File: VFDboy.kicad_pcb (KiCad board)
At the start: 2 copper layers, 141.2 x 60 mm, 161 parts, among them J1 AVR-ISP-6, J2 USB_C_Receptacle_USB2.0, J3 Micro_SD_Card_Det, J4 TagConnect_TC2030_SWD, Q1 FS8205A, Q2 S9015, Q3 AO3401A, Q4 AO3401A, Q5 S9015, Q6 2N7002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

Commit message: Add option for elevated D-Pad
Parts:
- added SW7: D-Pad, button-daughterboard:Daughterboard_D-Pad, F.Cu at (115.0, 129.9)
- moved D3 6.86 mm to (170.2, 104.1), turned to 180 degrees
- moved R2 3.01 mm to (168.0, 103.5), turned to 180 degrees
- moved R3 2.46 mm to (168.0, 104.6), turned to 180 degrees
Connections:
- U8 pad 42: /LEFT -> /DOWN
- U8 pad 43: /DOWN -> /LEFT
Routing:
- net Net-(D3-Pad2): track 12.4 -> 22.3 mm
- net +5V: track 508.2 -> 501.4 mm
- net /RIGHT: track 119.3 -> 121.7 mm
- net /DOWN: track 127.6 -> 125.4 mm
- net Net-(R2-Pad2): track 27.5 -> 29.4 mm
- net /LEFT: track 133.1 -> 134.4 mm
- net /UP: track 127.0 -> 126.3 mm
- net /Leds/Led 9/DIN: track 72.6 -> 72.0 mm
- net GND: vias 219 -> 272

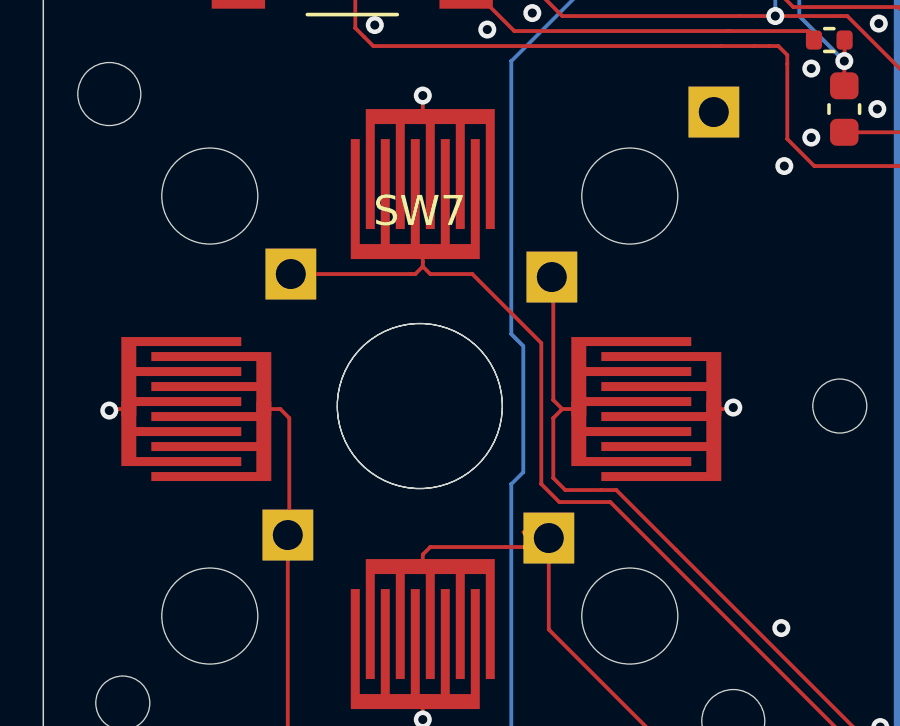
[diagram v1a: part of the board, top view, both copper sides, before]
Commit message: Hide silkscreen reference designators
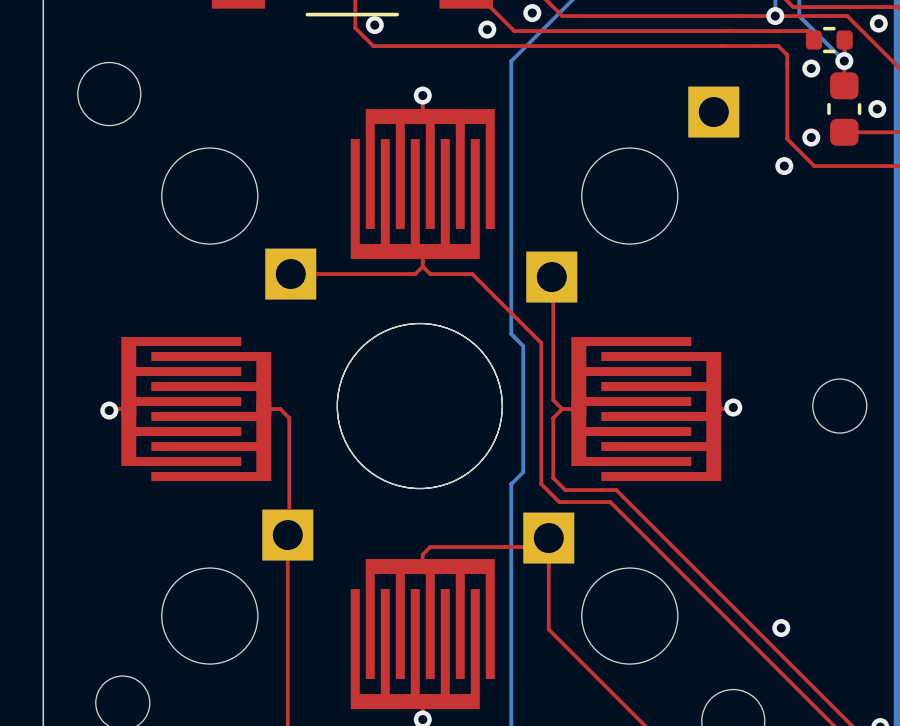
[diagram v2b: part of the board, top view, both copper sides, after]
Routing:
- net /DOWN: track 125.4 -> 124.8 mm

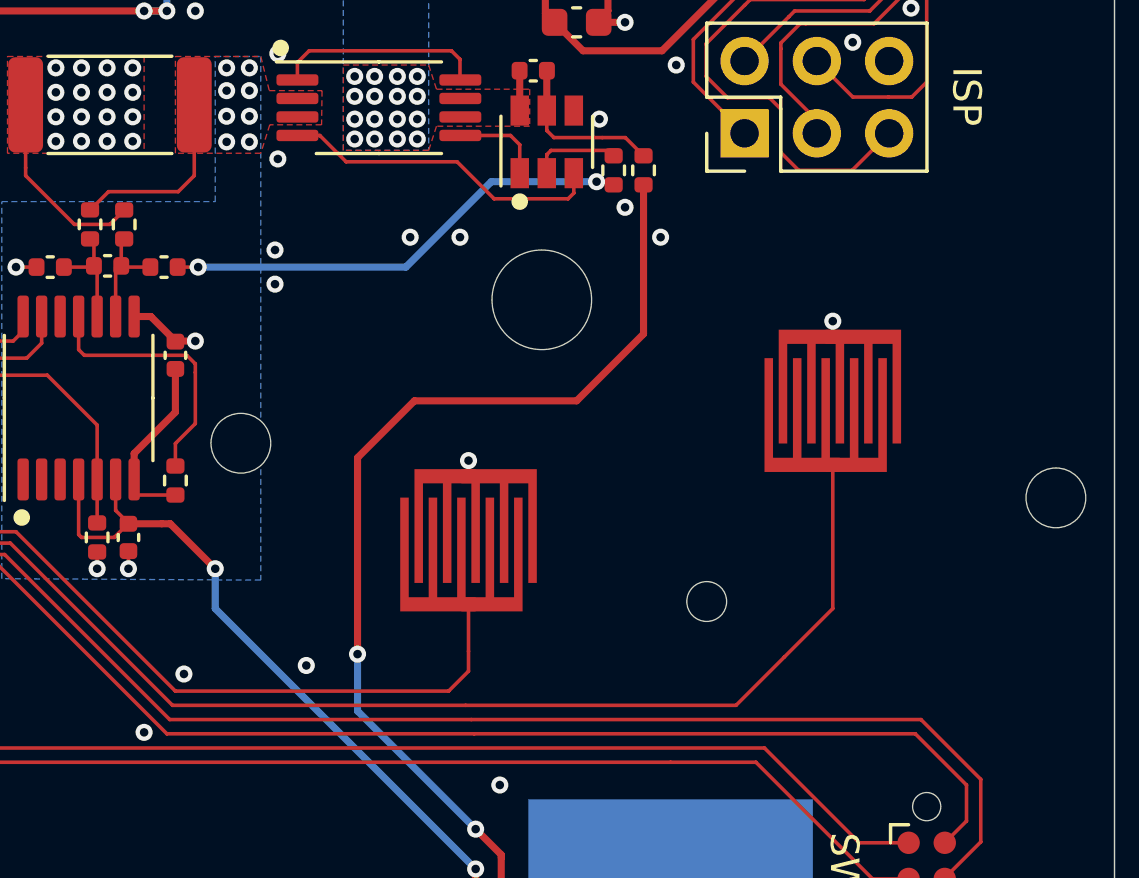
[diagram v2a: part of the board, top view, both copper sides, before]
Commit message: Implement elevated AB surfaces
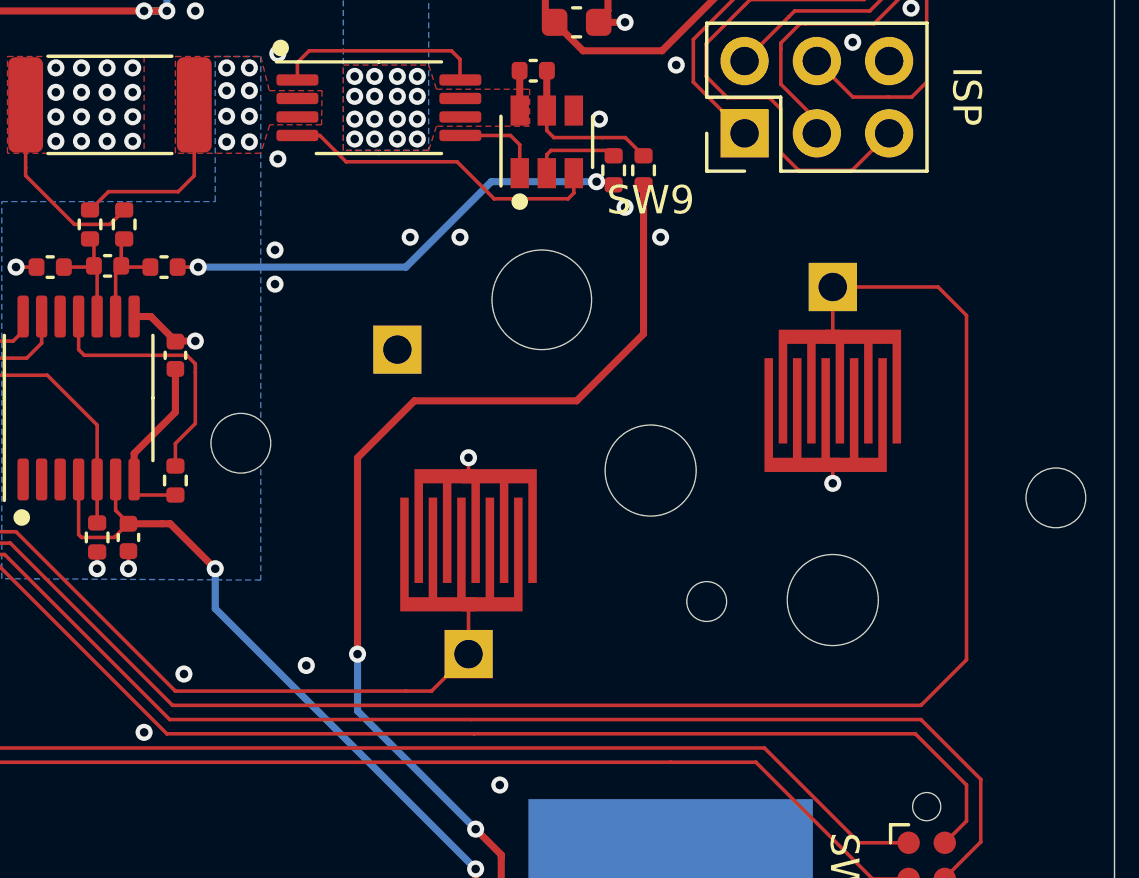
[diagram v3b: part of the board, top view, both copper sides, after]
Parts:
- added SW9: AB, button-daughterboard:Daugtherboard_AB, F.Cu at (227.3, 133.4)
- turned SW2 to 0 degrees
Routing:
- net /A: track 124.4 -> 142.2 mm

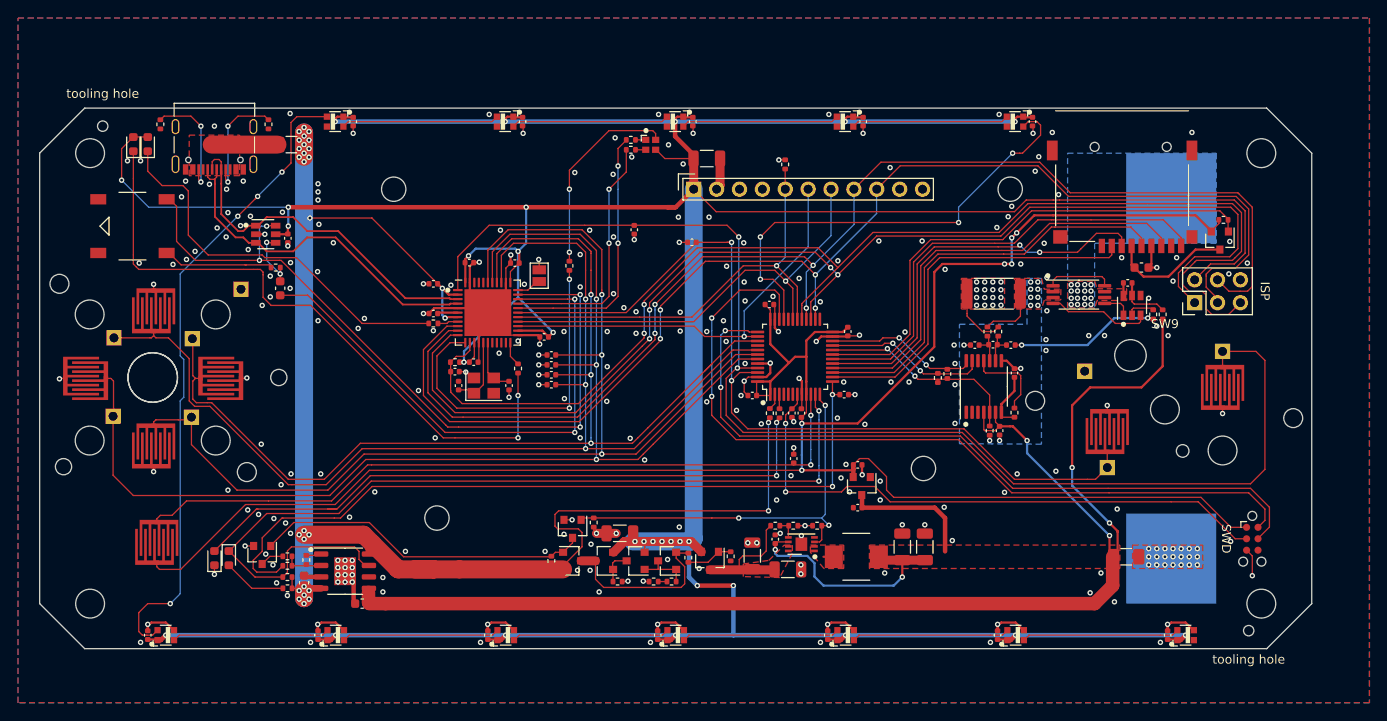
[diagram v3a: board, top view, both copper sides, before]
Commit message: Use tactile power switch
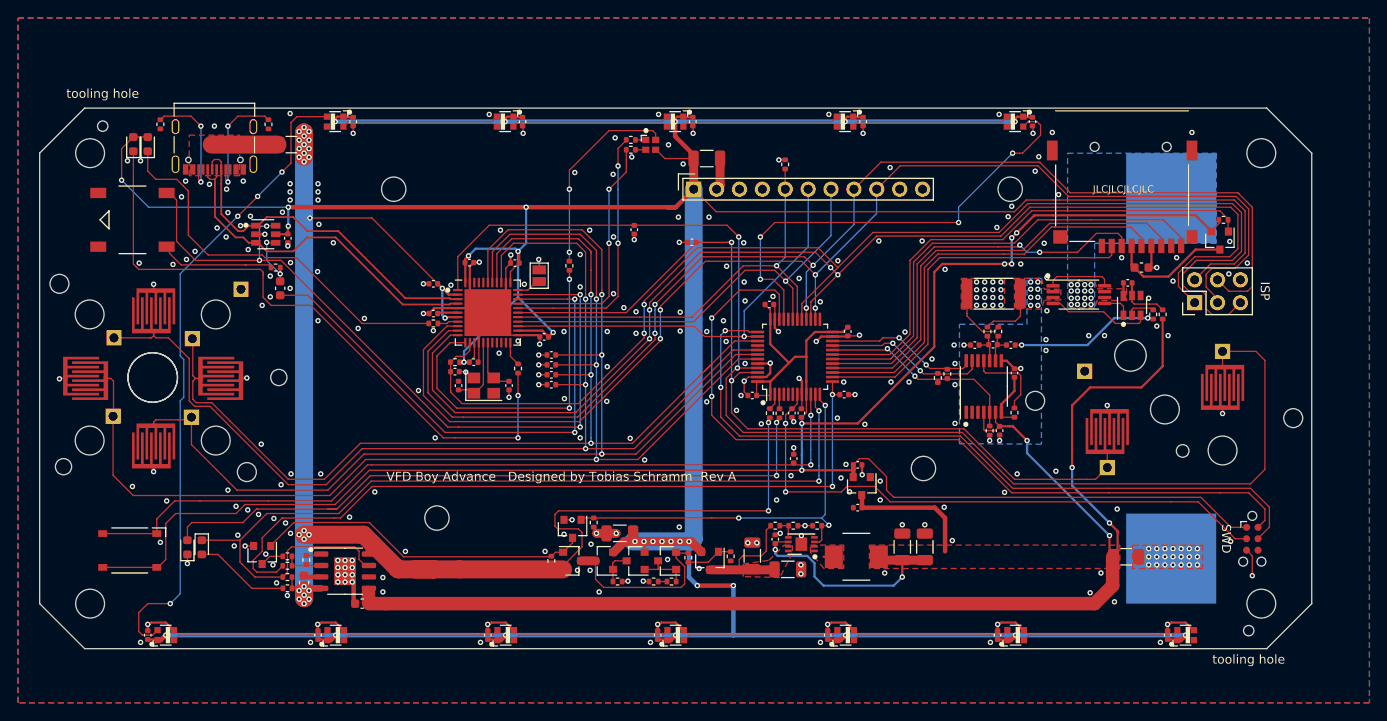
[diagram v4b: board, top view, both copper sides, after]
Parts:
- SW8: footprint Button_Carbon:Button_Carbon_5mm -> XKB_switch:TS-1187A-X-X-X
- moved D4 3.23 mm to (120.4, 148.8)
- moved D5 3.23 mm to (118.8, 148.8)
- moved SW8 3.13 mm to (112.4, 149.1), turned to 180 degrees
- moved LS1 0.70 mm to (112.7, 112.4)
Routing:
- net +3V3: track 236.0 -> 243.7 mm
- net Net-(C60-Pad1): track 83.5 -> 90.9 mm
- net Net-(D4-Pad2): track 7.06 -> 10.5 mm
- net Net-(D5-Pad2): track 73.3 -> 76.7 mm
- net /Power/LEDchg: track 99.5 -> 102.8 mm
- net /SPKR-: track 85.8 -> 86.5 mm
- net GND: vias 272 -> 281
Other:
- board text added: "JLCJLCJLCJLC"
- board text added: "Tobias Schramm"
- board text added: "VFD Boy Advance Designed by Tobias Schramm Rev A"

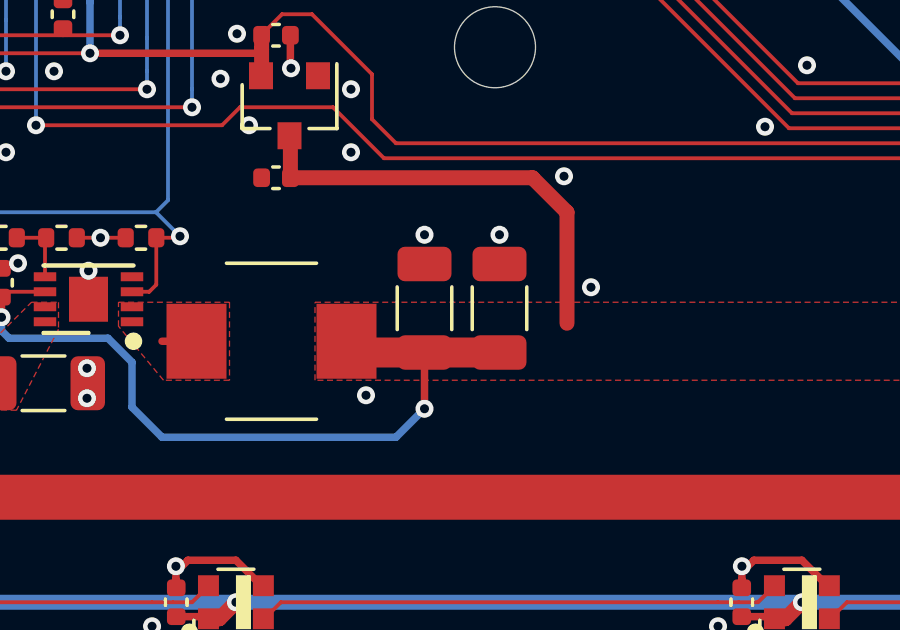
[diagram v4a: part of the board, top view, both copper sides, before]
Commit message: Reduce paste coverage on QFN and DFN thermal pads
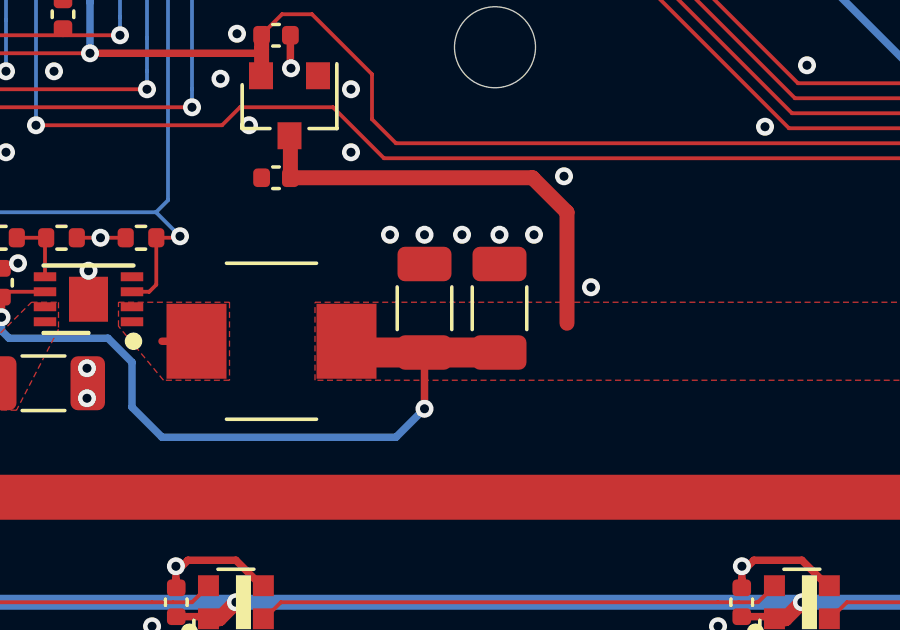
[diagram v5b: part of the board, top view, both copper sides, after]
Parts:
- U1: footprint Package_DFN_QFN:QFN-44-1EP_7x7mm_P0.5mm_EP5.2x5.2mm -> QFN_little_paste:QFN-44-1EP_7x7mm_P0.5mm_EP5.2x5.2mm_little_paste
- U3: footprint Package_DFN_QFN:DFN-8-1EP_3x2mm_P0.5mm_EP1.3x1.5mm -> DFN_little_paste:DFN-8-1EP_3x2mm_P0.5mm_EP1.3x1.5mm_little_paste
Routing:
- net GND: vias 281 -> 283

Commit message: Remove large name
JLCPCB does not support black solder resist + ENIG for assembly
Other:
- board text removed: "Tobias Schramm"
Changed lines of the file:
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@@
   (general
     (thickness 1.6)
-    (drawings 124)
+    (drawings 123)
     (tracks 1868)
     (zones 0)
@@
     (effects (font (size 0.8 0.8) (thickness 0.15)))
   )
-  (gr_text "Tobias Schramm" (at 147.4 104.6) (layer F.Mask)
-    (effects (font (size 2 2) (thickness 0.3)))
-  )
   (gr_circle (center 228.046 159.5) (end 227.904579 159.5) (layer F.SilkS) (width 0.3))
